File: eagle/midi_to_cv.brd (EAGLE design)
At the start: 100 x 80 mm, 45 parts, among them IC2 4504N, IC3 4099N, U1 ATMEGA328P_PDIP

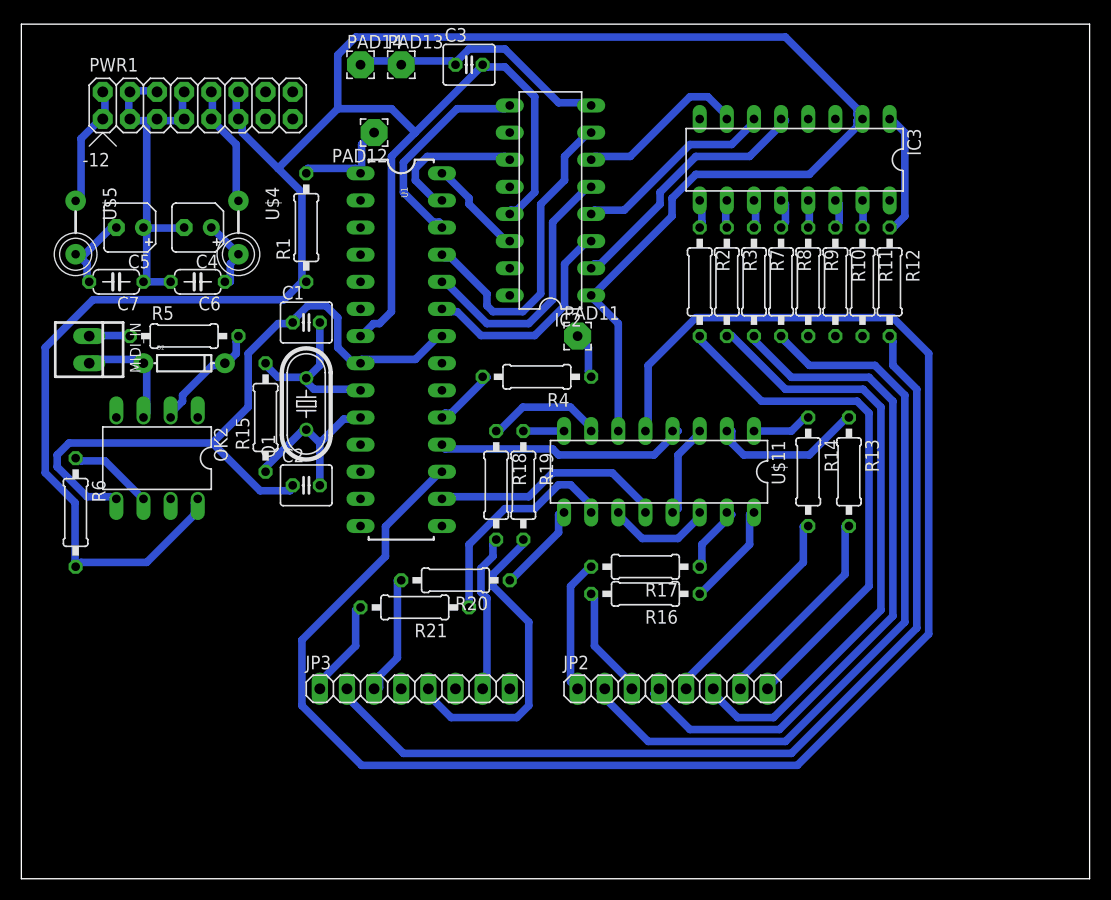
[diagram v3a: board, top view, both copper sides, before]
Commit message: connected midi to serial in
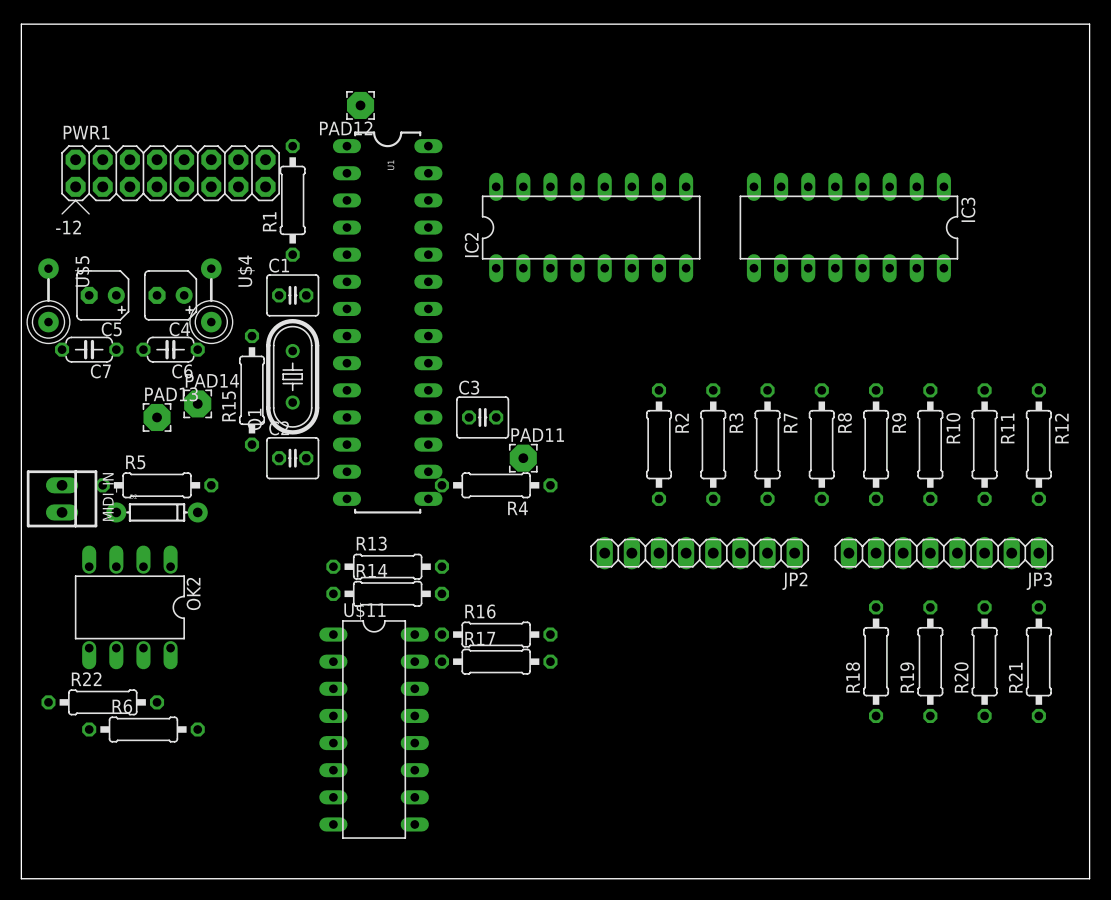
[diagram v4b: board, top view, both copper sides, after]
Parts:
- added R22: 2k4, rcl:0207/10
- moved R21 58.6 mm to (95.2, 20.3), turned to 90 degrees
- moved JP3 51.1 mm to (86.4, 30.5), turned to 180 degrees
- moved R20 50.1 mm to (90.2, 20.3), turned to 90 degrees
- moved R13 44.1 mm to (34.3, 29.2), turned to 0 degrees
- moved R19 41.5 mm to (85.1, 20.3), turned to 90 degrees
- moved R14 41.0 mm to (34.3, 26.7), turned to 0 degrees
- moved PAD13 40.2 mm to (12.7, 43.2)
- moved R18 39.2 mm to (80.0, 20.3), turned to 90 degrees
- moved U$11 36.0 mm to (33.0, 14.0), turned to 270 degrees
- moved PAD14 35.2 mm to (16.5, 44.5)
- moved C3 33.0 mm to (43.2, 43.2)
- moved R6 21.3 mm to (11.4, 14.0), turned to 0 degrees
- moved R12 20.7 mm to (95.2, 40.6)
- moved R11 19.1 mm to (90.2, 40.6)
- moved R10 17.6 mm to (85.1, 40.6)
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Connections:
- removed net N$30: U1.2
- new net N$60: OK2.7, R22.2
- new net N$61: IC2.15, IC3.2
- net +5V: no longer IC3.2
- net GND: now also R22.1
- net N$20: now also U1.2
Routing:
- net +5V: track 264.4 -> 0.00 mm
- net N$14: track 155.6 -> 0.00 mm
- net GND: track 101.8 -> 0.00 mm
- net N$21: track 89.7 -> 0.00 mm
- net N$8: track 70.7 -> 0.00 mm
- net N$7: track 64.6 -> 0.00 mm
- net N$6: track 57.4 -> 0.00 mm
- net N$3: track 48.7 -> 0.00 mm
- net N$26: track 34.5 -> 0.00 mm
- net N$31: track 30.0 -> 0.00 mm
- net N$41: track 29.5 -> 0.00 mm
- net N$25: track 25.2 -> 0.00 mm
- net N$33: track 25.0 -> 0.00 mm
- net N$27: track 24.0 -> 0.00 mm
- net N$15: track 22.1 -> 0.00 mm
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
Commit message: ever closer to a route
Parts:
- C3: value .1uF -> 100n
- moved U$5 91.7 mm to (94.0, 61.0)
- moved C7 81.6 mm to (87.6, 57.1), turned to 0 degrees
- moved C5 80.4 mm to (87.6, 62.2), turned to 0 degrees
- moved PWR1 76.4 mm to (87.6, 71.1), turned to 180 degrees
- moved C4 67.7 mm to (81.3, 62.2), turned to 0 degrees
- moved C6 67.7 mm to (81.3, 57.1), turned to 0 degrees
- moved U$4 57.5 mm to (74.9, 61.0)
- moved R6 53.6 mm to (24.1, 66.0), turned to 90 degrees
- moved R22 51.5 mm to (21.6, 66.0), turned to 90 degrees
- moved R20 49.3 mm to (41.9, 10.2)
- moved R21 47.1 mm to (49.5, 8.89), turned to 0 degrees
- moved OK2 40.8 mm to (14.0, 66.0), turned to 270 degrees
- moved D2 34.9 mm to (6.35, 68.6), turned to 90 degrees
- moved R5 31.8 mm to (3.81, 67.3), turned to 90 degrees
- moved R19 25.6 mm to (62.2, 8.89)
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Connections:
- removed net N$32 (its old number): IC2.9, U1.26
- removed net N$43: IC2.14, U1.28
- new net N$30: IC2.3, U1.25
- new net N$34: IC2.9, U1.28
- net N$23: now also IC2.7; no longer IC2.3
- net N$31: now also IC2.14, U1.26; no longer IC2.7, U1.25
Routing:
- net +5V: track 0.00 -> 252.0 mm
- net N$61: track 0.00 -> 193.9 mm
- net GND: track 0.00 -> 176.9 mm
- net +12V: track 0.00 -> 132.5 mm
- net N$29: track 0.00 -> 118.2 mm
- net N$50: track 0.00 -> 77.7 mm
- net N$42: track 0.00 -> 51.1 mm
- net N$51: track 0.00 -> 42.7 mm
- net N$41: track 0.00 -> 37.7 mm
- net N$57: track 0.00 -> 34.9 mm
- net N$27: track 0.00 -> 34.0 mm
- net N$35: track 0.00 -> 32.7 mm
- net N$26: track 0.00 -> 31.8 mm
- net N$56: track 0.00 -> 31.1 mm
- net N$15: track 0.00 -> 30.3 mm
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
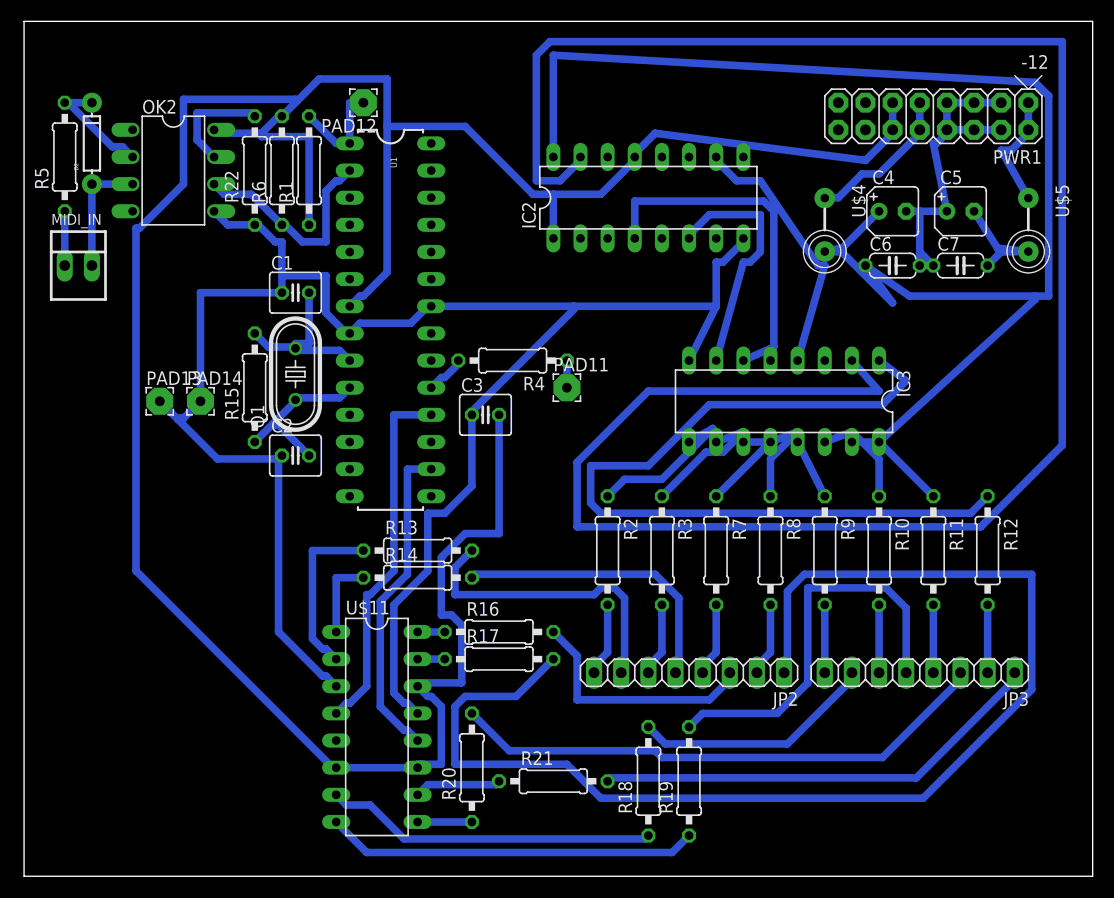
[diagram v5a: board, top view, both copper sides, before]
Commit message: 96 percent autorouting
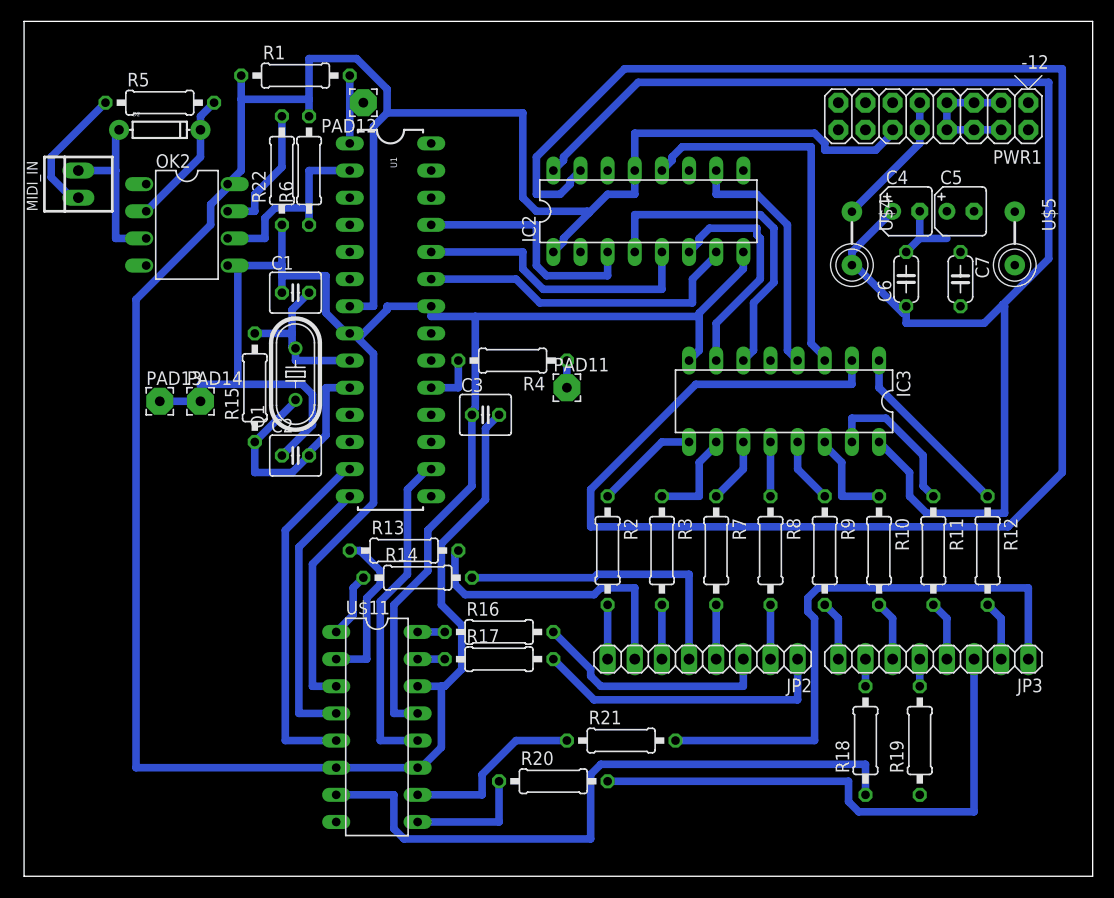
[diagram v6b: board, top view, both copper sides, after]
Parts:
- moved R19 21.9 mm to (83.8, 12.7)
- moved R18 20.7 mm to (78.7, 12.7)
- moved R5 10.2 mm to (12.7, 72.4), turned to 0 degrees
- moved R1 8.98 mm to (25.4, 74.9), turned to 0 degrees
- moved R20 7.73 mm to (49.5, 8.89), turned to 0 degrees
- moved MIDI_IN 7.62 mm to (5.08, 64.8), turned to 90 degrees
- moved R21 7.41 mm to (55.9, 12.7)
- moved D2 6.48 mm to (12.7, 69.8), turned to 0 degrees
- moved OK2 5.24 mm to (15.2, 61.0)
- moved U$4 2.84 mm to (77.5, 59.7)
- moved R6 2.54 mm to (26.7, 66.0)
- moved R22 2.54 mm to (24.1, 66.0)
- moved U$5 1.80 mm to (92.7, 59.7)
- moved JP3 1.80 mm to (85.1, 20.3)
- moved JP2 1.80 mm to (63.5, 20.3)
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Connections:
- removed net -12V: C5.-, C7.2, U$5.P$2
- new net N$62: PWR1.11, PWR1.12, U$5.P$1
- net +5V: no longer PWR1.11, PWR1.12
- net N$13: now also U$5.P$2; no longer PWR1.1, PWR1.2, U$5.P$1
- net N$14: now also U1.13; no longer U1.17
- net N$26: no longer C5.+, C7.1
- net N$27: now also U1.14; no longer U1.18
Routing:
- net N$29: track 118.2 -> 28.2 mm
- net N$50: track 77.7 -> 16.9 mm
- net N$38: track 0.00 -> 35.6 mm
- net N$41: track 37.7 -> 2.54 mm
- net N$57: track 34.9 -> 0.00 mm
- net N$14: track 0.00 -> 32.8 mm
- net N$56: track 31.1 -> 62.4 mm
- net N$23: track 0.00 -> 31.1 mm
- net N$25: track 0.00 -> 27.5 mm
- net N$30: track 0.00 -> 22.9 mm
- net N$40: track 22.8 -> 2.54 mm
- net N$61: track 193.9 -> 179.6 mm
- net N$26: track 31.8 -> 19.6 mm
- net N$51: track 42.7 -> 54.3 mm
- net -12V: track 11.3 -> 0.00 mm
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
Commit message: routed
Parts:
- moved PAD13 5.39 mm to (16.5, 40.6)
- moved R14 5.08 mm to (36.8, 33.0)
- moved R18 1.90 mm to (78.7, 10.8)
- moved R19 1.90 mm to (83.8, 10.8)
- moved R22 1.42 mm to (24.8, 64.8)
- moved R13 1.27 mm to (35.6, 29.2)
- moved R21 1.27 mm to (55.9, 11.4)
- moved R20 0.63 mm to (50.2, 8.89)
- moved R6 0.63 mm to (27.3, 66.0)
- moved JP3 0.63 mm to (85.7, 20.3)
- turned C1 to 180 degrees
- turned C5 to 180 degrees
- turned MIDI_IN to 0 degrees
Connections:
- removed net N$13: U$5.P$2
- net +5V: now also C5.+, C7.1, U$5.P$2
- net N$26: now also C5.-, C7.2
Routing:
- net +5V: track 247.8 -> 360.6 mm
- net N$61: track 179.6 -> 108.3 mm, vias 0 -> 2
- net N$57: track 0.00 -> 56.6 mm
- net +12V: track 132.8 -> 95.3 mm
- net N$34: track 0.00 -> 33.6 mm, vias 0 -> 2
- net N$62: track 0.00 -> 31.7 mm
- net N$33: track 0.00 -> 30.9 mm, vias 0 -> 2
- net N$32: track 0.00 -> 29.5 mm, vias 0 -> 2
- net GND: track 185.6 -> 162.6 mm
- net N$31: track 0.00 -> 18.4 mm, vias 0 -> 2
- net N$26: track 19.6 -> 34.7 mm
- net N$51: track 54.3 -> 39.9 mm
- net N$42: track 50.9 -> 41.2 mm
- net N$56: track 62.4 -> 53.8 mm
- net N$53: track 6.13 -> 12.0 mm
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
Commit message: mid nineties autoroute
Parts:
- moved PAD14 29.5 mm to (45.7, 48.3)
- moved R17 14.4 mm to (54.6, 10.2)
- moved U$4 13.1 mm to (83.8, 71.1)
- moved R20 12.5 mm to (61.6, 3.81)
- moved C6 12.0 mm to (78.7, 67.3), turned to 180 degrees
- moved R16 12.0 mm to (50.8, 12.7)
- moved C7 11.7 mm to (78.7, 63.5), turned to 180 degrees
- moved C4 10.9 mm to (78.7, 72.4), turned to 270 degrees
- moved C5 9.25 mm to (78.7, 59.7), turned to 90 degrees
- moved U$5 8.98 mm to (83.8, 61.0), turned to 90 degrees
- moved C3 7.73 mm to (41.9, 50.8), turned to 270 degrees
- moved PAD13 7.18 mm to (21.6, 35.6)
- moved PAD11 5.68 mm to (45.7, 43.2)
- moved R21 5.24 mm to (57.1, 6.35)
- moved PWR1 4.58 mm to (90.2, 67.3), turned to 270 degrees
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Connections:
- net N$33: now also IC2.6; no longer IC2.2
- net N$36: now also IC2.2; no longer IC2.6
- net N$37: now also IC3.3; no longer IC3.4
- net N$38: now also IC3.4; no longer IC3.3
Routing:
- net +5V: track 360.6 -> 0.00 mm
- net GND: track 162.6 -> 0.00 mm
- net N$61: track 108.3 -> 0.00 mm, vias 2 -> 0
- net +12V: track 95.3 -> 0.00 mm
- net N$57: track 56.6 -> 0.00 mm
- net N$56: track 53.8 -> 0.00 mm
- net N$42: track 41.2 -> 0.00 mm
- net N$38: track 40.0 -> 0.00 mm
- net N$51: track 39.9 -> 0.00 mm
- net N$15: track 35.3 -> 0.00 mm
- net N$26: track 34.7 -> 0.00 mm
- net N$30: track 33.6 -> 0.00 mm, vias 2 -> 0
- net N$13: track 32.2 -> 0.00 mm
- net N$62: track 31.7 -> 0.00 mm
- net N$33: track 30.9 -> 0.00 mm, vias 2 -> 0
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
